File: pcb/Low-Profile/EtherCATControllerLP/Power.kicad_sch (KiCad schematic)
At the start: 60 parts, among them U2 TPS54360DDAR, U3 LDL1117S33R, U4 LP5907MFX-3.3_NOPB, U8 LM76005RNPR

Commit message: checkpoint
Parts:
- removed C13, C14, C80: 2.2uF, symbol Device:C_Small
- removed C15: 39pF, symbol Device:C_Small
- removed C16, C17, C18: 4.7uF, Capacitor_SMD:C_0805_2012Metric, symbol Device:C
- removed C37, C38, C39, C55: 0.1uF, symbol Device:C
- removed C74: 6800pF, symbol Device:C_Small
- removed C75: 0.1uF, symbol Device:C_Small
- removed C76, C77: 47uF, symbol Device:C_Small
- removed C78: 4.7pF, symbol Device:C_Small
- removed C79, C81, C83: 470nF, symbol Device:C_Small
- removed C82: 150uF, symbol Device:C_Small
- removed D1: LTST-C190KGKT, Diode_SMD:D_0603_1608Metric, symbol LTST-C190KGKT:LTST-C190KGKT
- removed D2: B560C, symbol Device:D_Schottky
- removed L1: 8.2uH, symbol Device:L_Small
- removed L2: 5.6uH, symbol Device:L_Small
- removed R1: 523K, symbol Device:R_Small
- removed R2: 162K, symbol Device:R_Small
- removed R3: 84.5, symbol Device:R_Small
- removed R38: 53.6K, symbol Device:R_Small
- removed R39: 10.2K, symbol Device:R_Small
- removed R4: 13K, symbol Device:R_Small
- removed R40: 100k, symbol Device:R_Small
- removed R41: 100K, symbol Device:R_Small
- removed R42: 43.2K, symbol Device:R_Small
- removed R5: 1k, Resistor_SMD:R_0603_1608Metric, symbol Device:R
- removed TP2, TP3, TP5: TESTPOINT, TestPoint:TestPoint_Pad_1.0x1.0mm, symbol Connector:TestPoint
- removed U2: TPS54360DDAR, Package_SO:TI_SO-PowerPAD-8_ThermalVias, symbol Regulator_Switching:TPS54360DDA
- removed U3: LDL1117S33R, Package_TO_SOT_SMD:SOT-223, symbol LDL1117S33R:LDL1117S33R
- removed U4: LP5907MFX-3.3_NOPB, Package_TO_SOT_SMD:SOT-23-5, symbol LP5907MFX-3.3_NOPB:LP5907MFX-3.3_NOPB
- removed U8: LM76005RNPR, RNP0030A, symbol 2024-07-02_05-34-37:LM76005RNPR
- added C10, C5, C6, C9: 10uF, symbol Device:C
- added C77, C79, C80, C81: 0.1uF, symbol Device:C
- C1, C2, C3, C4: LCSC Part # (none) -> C153035; LCSC Part Number C153035 -> (none)
- C40: LCSC Part # (none) -> C77183
- C41: value ${CAPACITANCE} -> 2.2uF; LCSC Part # (none) -> C77183
- C42, C56, C57: LCSC Part # (none) -> C14663
- C43, C44, C45, C46: LCSC Part # (none) -> C77055
- C7, C8: LCSC Part # (none) -> C1921234; LCSC Part Number C1921234 -> (none)
- R23: LCSC Part # (none) -> C98220
- R24: LCSC Part # (none) -> C22548
- TP1, TP4: now not fitted
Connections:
- net AVCC: no longer TP1.1
- net DCBUS: now also TP1.1, C10.1, C5.1, C6.1, C9.1
- net EtherCAT3v3: now also C77.1, C79.1, C80.1, C81.1
- net GND: now also C10.2, C5.2, C6.2, C77.2, C79.2, C80.2, C81.2, C9.2
- no-connect marks 9 -> 0
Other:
- added sheet Regulators (Regulators.kicad_sch)
- note added: "AVCC supplied by MCF8329A"
- note removed: "5V out"
- note removed: "Analog 3v3"
- note removed: "Digital 3v3"
- note removed: "EtherCAT 3v3"
- moved on the sheet: C1, C2, C3, C4, C40, C41, C42, C43, C44, C45, C46, C7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

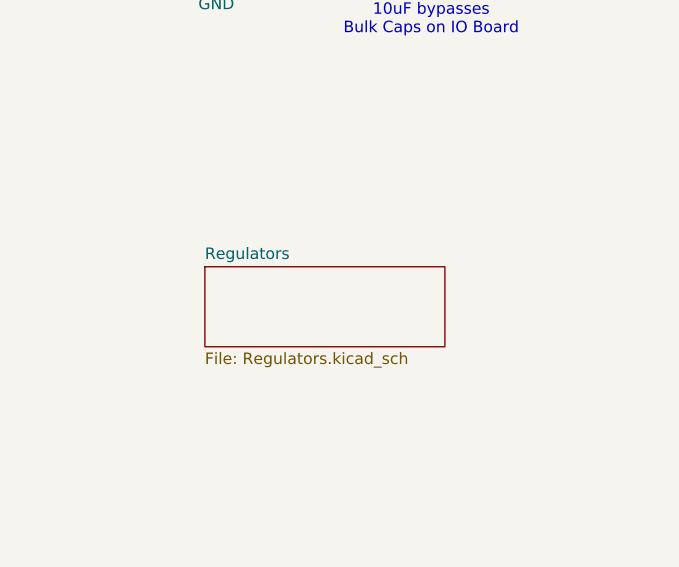
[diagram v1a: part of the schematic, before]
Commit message: Checkpoint changes before switching to XMC4800
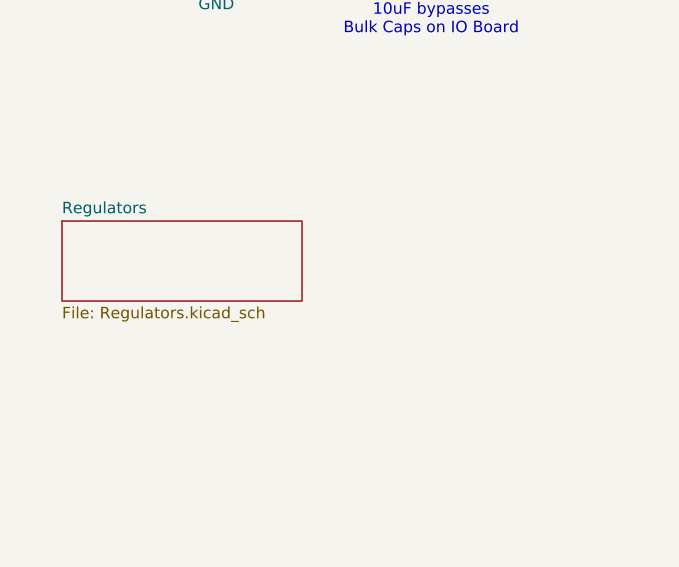
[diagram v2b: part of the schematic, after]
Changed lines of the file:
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@@
 	)
 	(sheet
-		(at 46.99 77.47)
+		(at 31.115 72.39)
 		(size 26.67 8.89)
 		(fields_autoplaced yes)
@@
 		)
 		(property "Sheetname" "Regulators"
-			(at 46.99 76.7584 0)
+			(at 31.115 71.6784 0)
 			(effects
 				(font
@@
 		)
 		(property "Sheetfile" "Regulators.kicad_sch"
-			(at 46.99 86.9446 0)
+			(at 31.115 81.8646 0)
 			(effects
 				(font

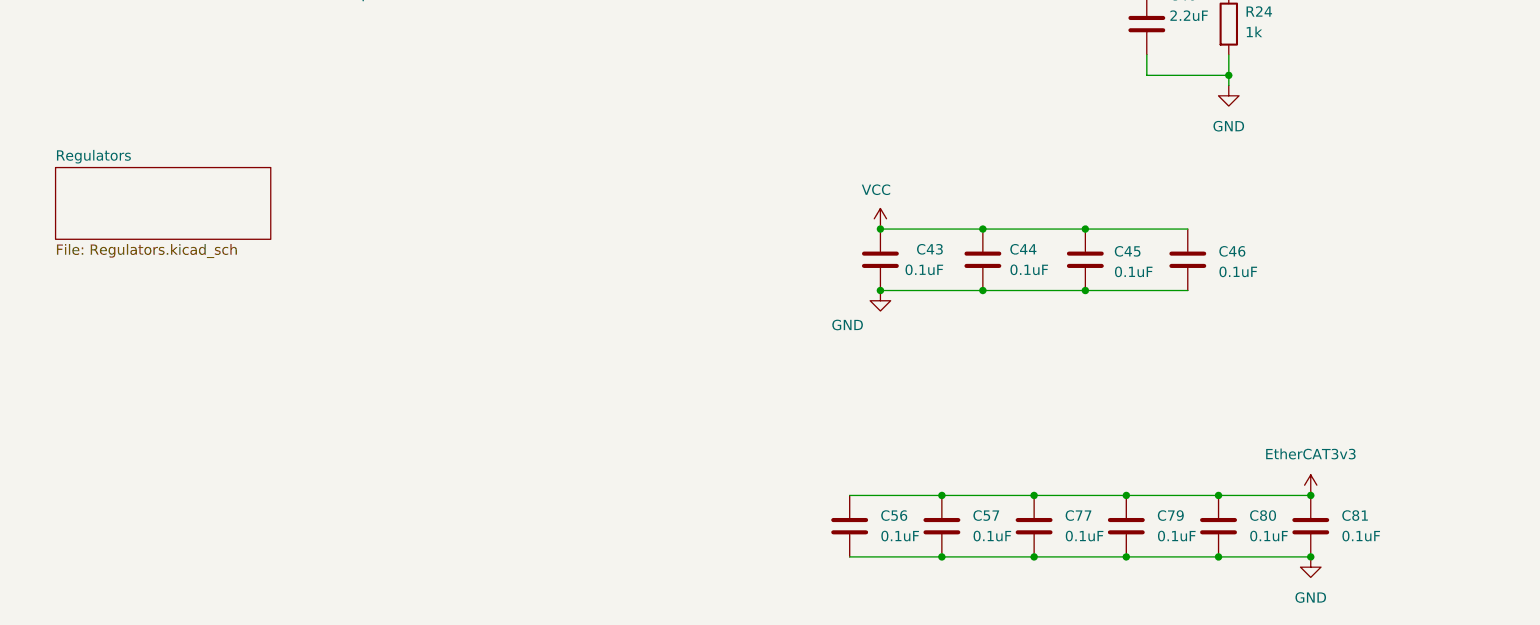
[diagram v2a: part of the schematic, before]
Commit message: Added XMC4800
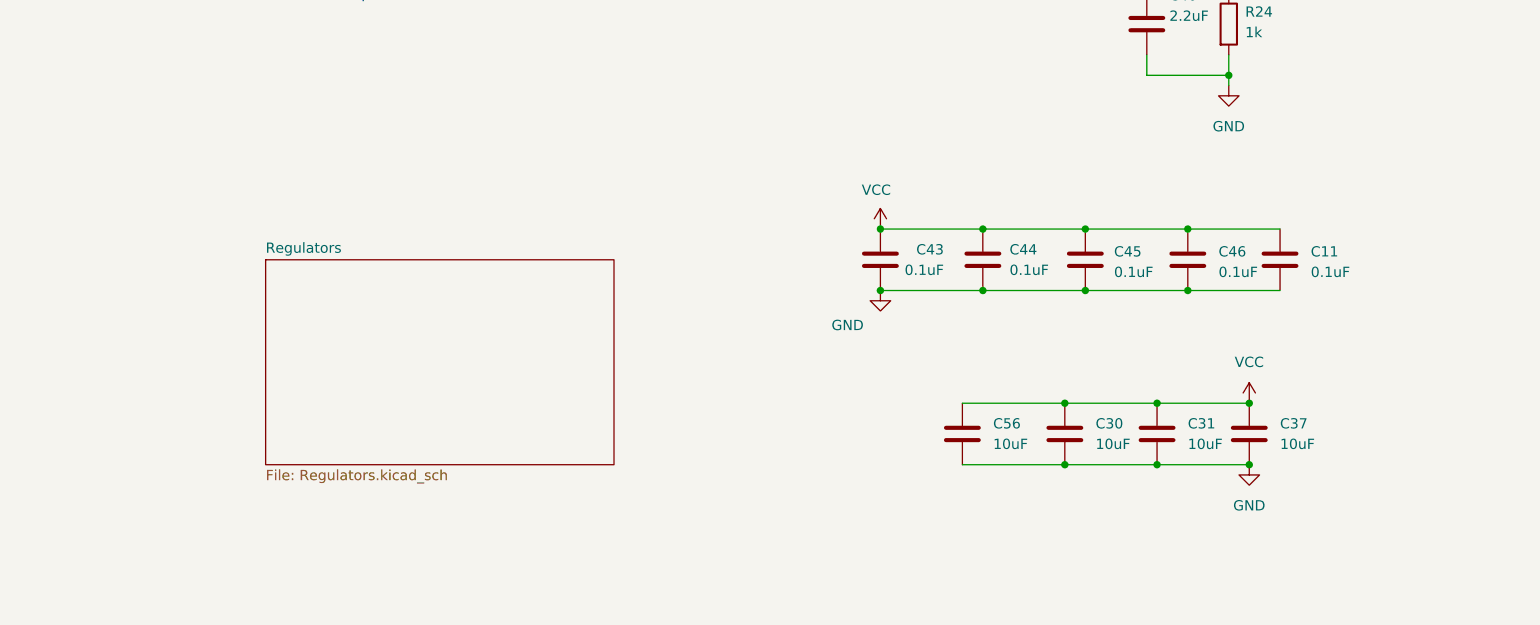
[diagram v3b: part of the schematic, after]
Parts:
- removed C57, C77, C79, C80, C81: 0.1uF, symbol Device:C
- added C11: ${CAPACITANCE}, Capacitor_SMD:C_0603_1608Metric, symbol Device:C
- added C30, C31, C37: 10uF, symbol Device:C
- C56: value 0.1uF -> 10uF; LCSC Part # C14663 -> C77075
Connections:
- net EtherCAT3v3 is gone; now on net VCC: C56.1
- net GND: now also C11.2, C30.2, C31.2, C37.2
- net VCC: now also C11.1, C30.1, C31.1, C37.1
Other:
- moved on the sheet: C56
